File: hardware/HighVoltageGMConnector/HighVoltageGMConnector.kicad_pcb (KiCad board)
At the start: 2 copper layers, 40 x 70 mm, 16 parts, among them J1 Conn_01x02_Male, J2 Conn_01x01_Female, J3 Conn_01x01_Female, J4 Conn_01x01_Female, J5 Conn_01x01_Female, J6 Conn_01x01_Female, J7 Conn_01x01_Female, J8 Conn_01x01_Female

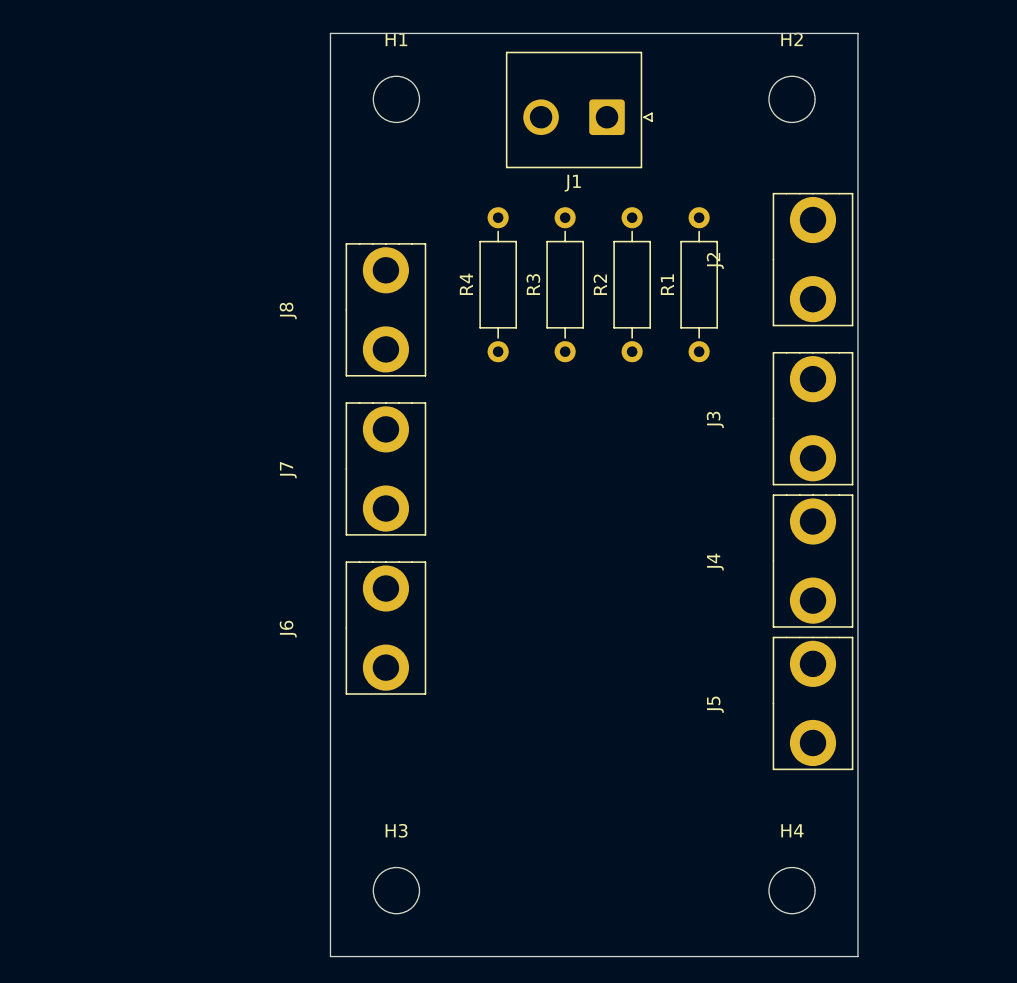
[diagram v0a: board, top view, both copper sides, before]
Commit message: fully routed
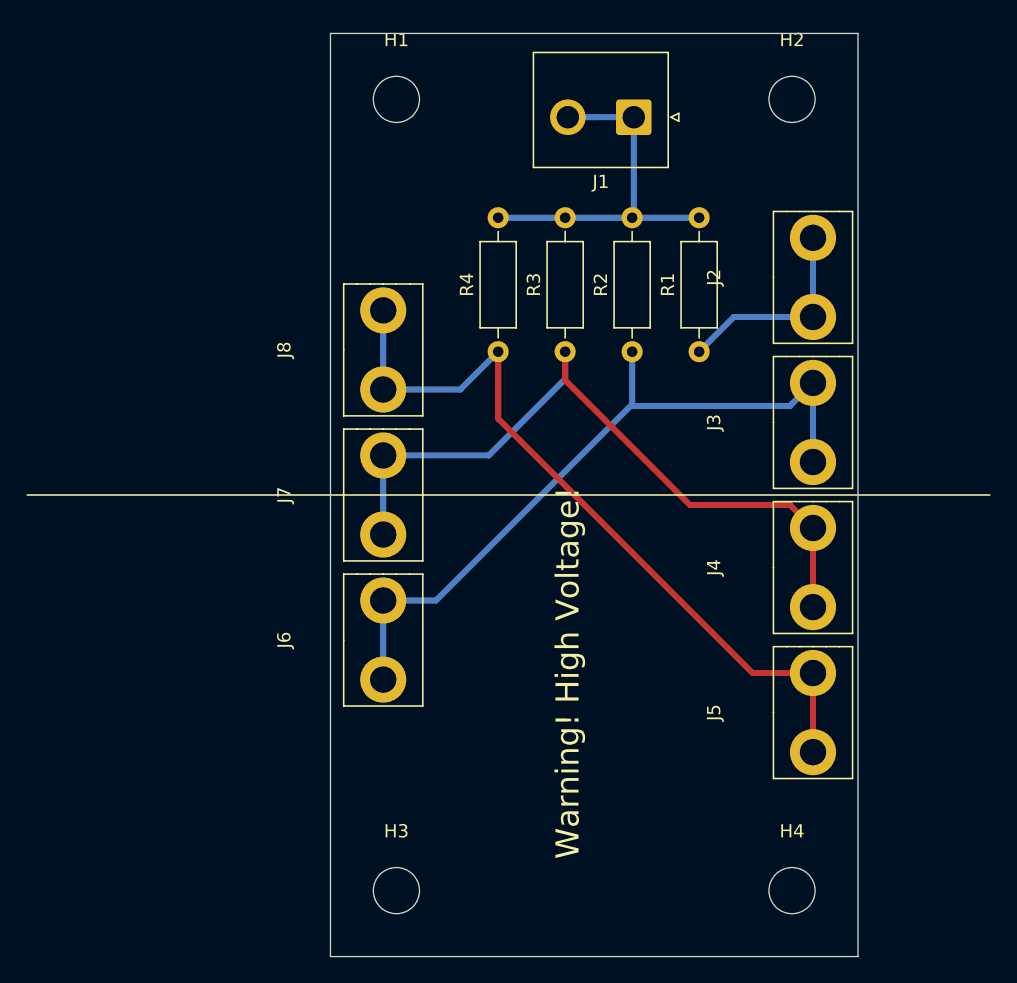
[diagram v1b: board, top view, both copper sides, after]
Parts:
- moved J8 3.05 mm to (116.0, 64.0)
- moved J1 2.03 mm to (143.0, 46.4)
- moved J7 1.99 mm to (116.0, 75.0)
- moved J2 1.35 mm to (148.6, 58.5)
- moved J6 0.93 mm to (116.0, 86.0)
- moved J5 0.69 mm to (148.6, 91.5)
- moved J4 0.49 mm to (148.6, 80.5)
- moved J3 0.28 mm to (148.6, 69.5)
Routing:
- net Net-(J5-Pad1): track 0.00 -> 58.8 mm
- net Net-(J4-Pad1): track 0.00 -> 55.9 mm
- net Net-(J3-Pad1): track 0.00 -> 55.5 mm
- net Net-(J1-Pad1): track 0.00 -> 27.9 mm
- net Net-(J2-Pad1): track 0.00 -> 15.7 mm
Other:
- board text added: "Warning! High Voltage!"
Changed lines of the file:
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@@
   (general
     (thickness 1.6)
-    (drawings 4)
-    (tracks 0)
+    (drawings 9)
+    (tracks 41)
     (zones 0)
     (modules 16)
@@
   )
   (setup
-    (last_trace_width 0.25)
+    (last_trace_width 0.4572)
+    (user_trace_width 0.4572)
     (trace_clearance 0.2)
     (zone_clearance 0.508)
@@
     (solder_mask_min_width 0.25)
     (aux_axis_origin 0 0)
-    (visible_elements FFFFFF7F)
+    (visible_elements 7FFFFFFF)
     (pcbplotparams
       (layerselection 0x010fc_ffffffff)
@@
   )
   (module CosmicRayDetector:GeigerTube (layer F.Cu)
-    (at 116.205 60.96 90)
+    (at 116 64 90)
     (fp_text reference J8 (at 0 0.5 90) (layer F.SilkS)
       (effects (font (size 1 1) (thickness 0.15)))
@@
   )
   (module CosmicRayDetector:GeigerTube (layer F.Cu)
-    (at 116.205 73.025 90)
+    (at 116 75 90)
     (fp_text reference J7 (at 0 0.5 90) (layer F.SilkS)
       (effects (font (size 1 1) (thickness 0.15)))
@@
   )
   (module CosmicRayDetector:GeigerTube (layer F.Cu)
-    (at 116.205 85.09 90)
+    (at 116 86 90)
     (fp_text reference J6 (at 0 0.5 90) (layer F.SilkS)
       (effects (font (size 1 1) (thickness 0.15)))
@@
   )
   (module CosmicRayDetector:GeigerTube (layer F.Cu)
-    (at 148.59 90.805 90)
+    (at 148.59 91.5 90)
     (fp_text reference J5 (at 0 0.5 90) (layer F.SilkS)
       (effects (font (size 1 1) (thickness 0.15)))
@@
   )
   (module CosmicRayDetector:GeigerTube (layer F.Cu)
-    (at 148.59 80.01 90)
+    (at 148.59 80.5 90)
     (fp_text reference J4 (at 0 0.5 90) (layer F.SilkS)
       (effects (font (size 1 1) (thickness 0.15)))
@@
   )
   (module CosmicRayDetector:GeigerTube (layer F.Cu)
-    (at 148.59 69.215 90)
+    (at 148.59 69.5 90)
     (fp_text reference J3 (at 0 0.5 90) (layer F.SilkS)
       (effects (font (size 1 1) (thickness 0.15)))
@@
   )
   (module CosmicRayDetector:GeigerTube (layer F.Cu)
-    (at 148.59 57.15 90)
+    (at 148.59 58.5 90)
     (fp_text reference J2 (at 0 0.5 90) (layer F.SilkS)
       (effects (font (size 1 1) (thickness 0.15)))
@@
   )
   (module Connector_JST:JST_NV_B02P-NV_1x02_P5.00mm_Vertical (layer F.Cu)
-    (at 140.97 46.355 180)
+    (at 143 46.355 180)
     (descr "JST NV series connector, B02P-NV (http://www.jst-mfg.com/product/pdf/eng/eNV.pdf), generated with kicad-footprint-generator")
     (tags "connector JST NV side entry")
@@
     )
   )
+  (gr_text "Warning! High Voltage!" (at 138 89 90) (layer B.SilkS)
+    (effects (font (size 1.75 1.75) (thickness 0.35)) (justify mirror))
+  )
+  (gr_text "Warning! High Voltage!" (at 138 88.5 90) (layer F.SilkS)
+    (effects (font (size 1.75 1.75) (thickness 0.35)))
+  )
+  (dimension 20 (width 0.12) (layer F.SilkS)
+    (gr_text "20.000 mm" (at 130 31.73) (layer F.SilkS)
+      (effects (font (size 1 1) (thickness 0.15)))
+    )
+    (feature1 (pts (xy 140 40) (xy 140 32.413579)))
+    (feature2 (pts (xy 120 40) (xy 120 32.413579)))
+    (crossbar (pts (xy 120 33) (xy 140 33)))
+    (arrow1a (pts (xy 140 33) (xy 138.873496 33.586421)))
+    (arrow1b (pts (xy 140 33) (xy 138.873496 32.413579)))
+    (arrow2a (pts (xy 120 33) (xy 121.126504 33.586421)))
+    (arrow2b (pts (xy 120 33) (xy 121.126504 32.413579)))
+  )
+  (gr_line (start 170 75) (end 97 75) (layer F.SilkS) (width 0.12))
+  (dimension 70 (width 0.12) (layer F.SilkS)
+    (gr_text "70.000 mm" (at 186.27 75 90) (layer F.SilkS)
+      (effects (font (size 1 1) (thickness 0.15)))
+    )
+    (feature1 (pts (xy 160 40) (xy 185.586421 40)))
+    (feature2 (pts (xy 160 110) (xy 185.586421 110)))
+    (crossbar (pts (xy 185 110) (xy 185 40)))
+    (arrow1a (pts (xy 185 40) (xy 185.586421 41.126504)))
+    (arrow1b (pts (xy 185 40) (xy 184.413579 41.126504)))
+    (arrow2a (pts (xy 185 110) (xy 185.586421 108.873496)))
+    (arrow2b (pts (xy 185 110) (xy 184.413579 108.873496)))
+  )
   (gr_line (start 120 110) (end 160 110) (layer Edge.Cuts) (width 0.05))
   (gr_line (start 120 40) (end 120 110) (layer Edge.Cuts) (width 0.05))
   (gr_line (start 160 40) (end 120 40) (layer Edge.Cuts) (width 0.05))
   (gr_line (start 160 40) (end 160 110) (layer Edge.Cuts) (width 0.05))
+  (segment (start 139.909188 46.355) (end 143 46.355) (width 0.4572) (layer B.Cu) (net 1))
+  (segment (start 138 46.355) (end 139.909188 46.355) (width 0.4572) (layer B.Cu) (net 1))
+  (segment (start 143 53.85) (end 142.875 53.975) (width 0.4572) (layer B.Cu) (net 1))
+  (segment (start 143 46.355) (end 143 53.85) (width 0.4572) (layer B.Cu) (net 1))
+  (segment (start 147.955 53.975) (end 142.875 53.975) (width 0.4572) (layer B.Cu) (net 1))
+  (segment (start 142.875 53.975) (end 137.795 53.975) (width 0.4572) (layer B.Cu) (net 1))
+  (segment (start 137.795 53.975) (end 132.715 53.975) (width 0.4572) (layer B.Cu) (net 1))
+  (segment (start 156.59 57.974873) (end 156.59 61.5) (width 0.4572) (layer B.Cu) (net 2))
+  (segment (start 156.59 55.5) (end 156.59 57.974873) (width 0.4572) (layer B.Cu) (net 2))
+  (segment (start 150.59 61.5) (end 147.955 64.135) (width 0.4572) (layer B.Cu) (net 2))
+  (segment (start 156.59 61.5) (end 150.59 61.5) (width 0.4572) (layer B.Cu) (net 2))
+  (segment (start 124 89) (end 124 83) (width 0.4572) (layer B.Cu) (net 3))
+  (segment (start 124 83) (end 128 83) (width 0.4572) (layer B.Cu) (net 3))
+  (segment (start 142.875 68.125) (end 142.875 64.135) (width 0.4572) (layer B.Cu) (net 3))
+  (segment (start 128 83) (end 142.875 68.125) (width 0.4572) (layer B.Cu) (net 3))
+  (segment (start 156.59 70.025127) (end 156.59 66.5) (width 0.4572) (layer B.Cu) (net 3))
+  (segment (start 156.59 72.5) (end 156.59 70.025127) (width 0.4572) (layer B.Cu) (net 3))
+  (segment (start 142.999999 68.249999) (end 142.875 68.125) (width 0.4572) (layer B.Cu) (net 3))
+  (segment (start 154.840001 68.249999) (end 142.999999 68.249999) (width 0.4572) (layer B.Cu) (net 3))
+  (segment (start 156.59 66.5) (end 154.840001 68.249999) (width 0.4572) (layer B.Cu) (net 3))
+  (segment (start 124 75.525127) (end 124 72) (width 0.4572) (layer B.Cu) (net 4))
+  (segment (start 124 78) (end 124 75.525127) (width 0.4572) (layer B.Cu) (net 4))
+  (segment (start 137.795 66.205) (end 137.795 64.135) (width 0.4572) (layer B.Cu) (net 4))
+  (segment (start 124 72) (end 132 72) (width 0.4572) (layer B.Cu) (net 4))
+  (segment (start 132 72) (end 137.795 66.205) (width 0.4572) (layer B.Cu) (net 4))
+  (segment (start 156.59 81.025127) (end 156.59 77.5) (width 0.4572) (layer F.Cu) (net 4))
+  (segment (start 156.59 83.5) (end 156.59 81.025127) (width 0.4572) (layer F.Cu) (net 4))
+  (segment (start 154.840001 75.750001) (end 147.250001 75.750001) (width 0.4572) (layer F.Cu) (net 4))
+  (segment (start 156.59 77.5) (end 154.840001 75.750001) (width 0.4572) (layer F.Cu) (net 4))
+  (segment (start 137.795 66.295) (end 137.795 64.135) (width 0.4572) (layer F.Cu) (net 4))
+  (segment (start 147.250001 75.750001) (end 137.795 66.295) (width 0.4572) (layer F.Cu) (net 4))
+  (segment (start 124 63.474873) (end 124 67) (width 0.4572) (layer B.Cu) (net 5))
+  (segment (start 124 61) (end 124 63.474873) (width 0.4572) (layer B.Cu) (net 5))
+  (segment (start 129.85 67) (end 132.715 64.135) (width 0.4572) (layer B.Cu) (net 5))
+  (segment (start 124 67) (end 129.85 67) (width 0.4572) (layer B.Cu) (net 5))
+  (segment (start 156.59 92.025127) (end 156.59 88.5) (width 0.4572) (layer F.Cu) (net 5))
+  (segment (start 156.59 94.5) (end 156.59 92.025127) (width 0.4572) (layer F.Cu) (net 5))
+  (segment (start 132.715 65.26637) (end 132.715 64.135) (width 0.4572) (layer F.Cu) (net 5))
+  (segment (start 132.715 69.215) (end 132.715 65.26637) (width 0.4572) (layer F.Cu) (net 5))
+  (segment (start 156.59 88.5) (end 152 88.5) (width 0.4572) (layer F.Cu) (net 5))
+  (segment (start 152 88.5) (end 132.715 69.215) (width 0.4572) (layer F.Cu) (net 5))
 )
